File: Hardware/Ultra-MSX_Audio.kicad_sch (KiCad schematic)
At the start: 25 parts, among them J14 Ultra-AUDIO-daughter, U23 S29GL128S90TFI010, U24 FXMA108, U25 FXMA108, U26 FXMA108, U27 FXMA108, U4 YM2610, U9 DAC_YM3016

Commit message: Finished the VDP-board, finished up the mixer-section, removed the buffer-pins from the FPGA, and instead added external buffers for the slots, designed a marquee-block with the Ultra-MSX logo, designed the logotype, andmultiple other changes.
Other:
- note added: "SPI to Parallel (for using modern ROM's) https://highfieldtales.wordpress.com/2011/12/04/very-fast-spi-to-parallel-interface-for-netduino/ -- FPGA-implementation of YM2610: https://github.com/jotego/jt12 YM3016: The YM3015 is nearly identical, except voltage-levels, hence it can be used to figure out a replacement. http://gendev.spritesmind.net/forum/viewtopic.php?t=386&start=180"
- note removed: "SPI to Parallel (for using modern ROM's) https://highfieldtales.wordpress.com/2011/12/04/very-fast-spi-to-parallel-interface-for-netduino/ How to build an Audio mixer: https://www.circuitlib.com/index.php/tutorials/product/39-how-to-build-an-audio-mixer How to inject Mono into Stereo-output; Build a Virtual Earth Summing Amp "Make sure you use linear taper pots for the pans and audio taper pots f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"

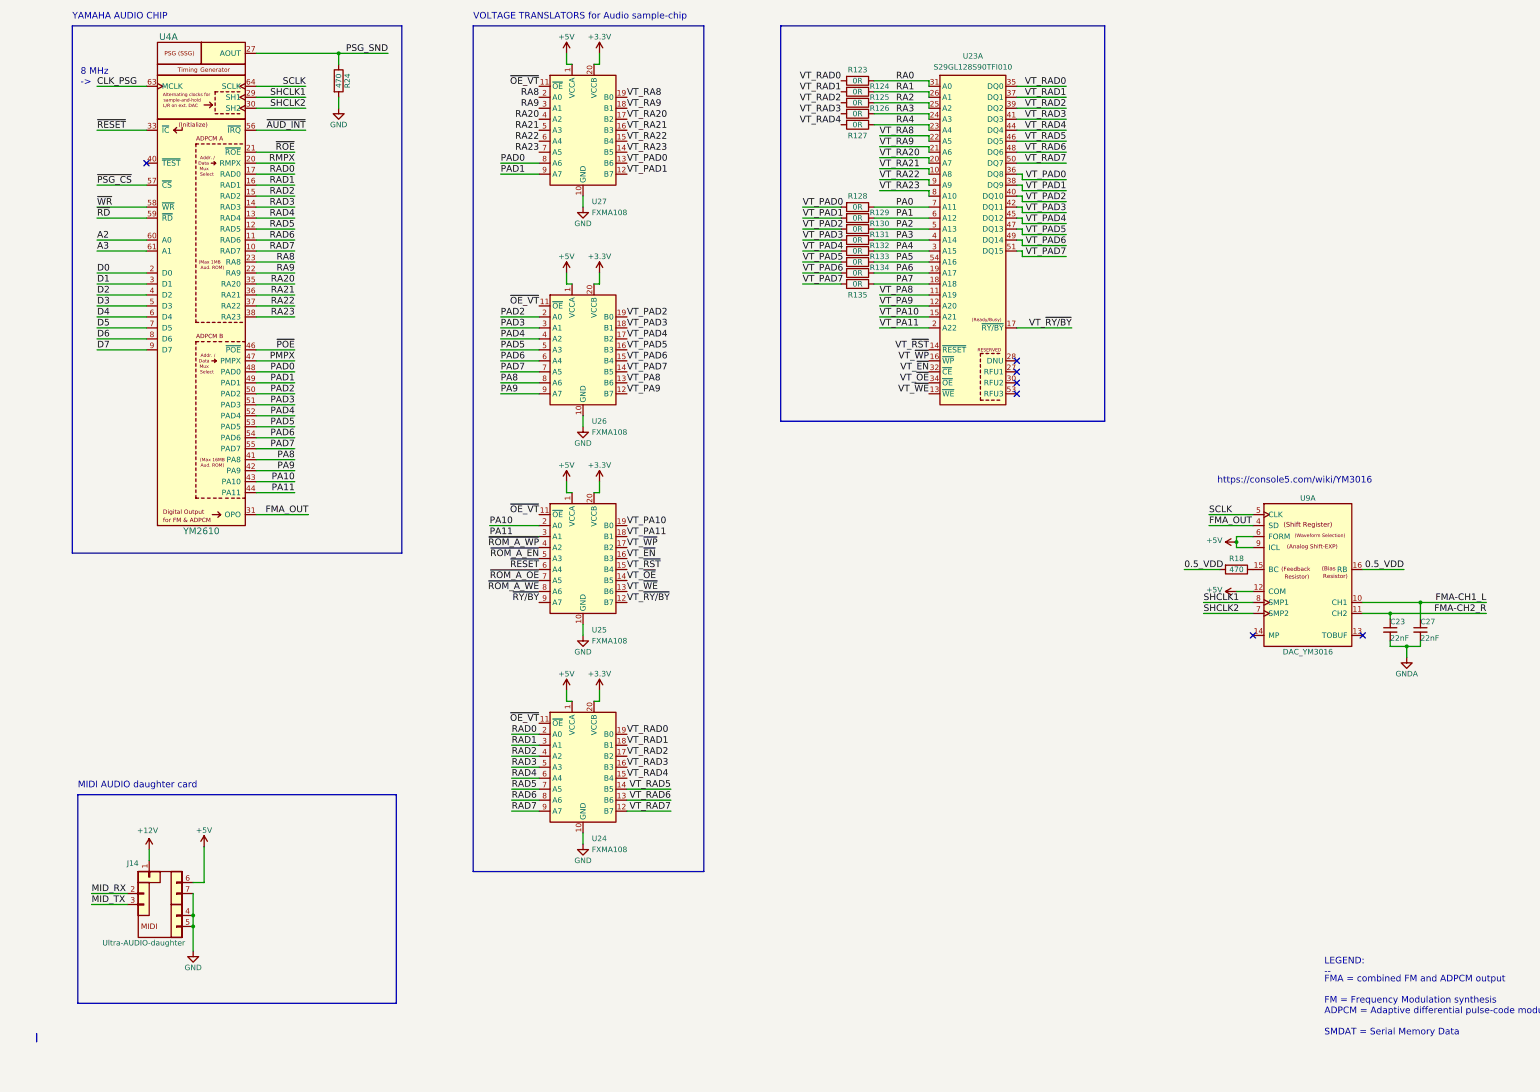
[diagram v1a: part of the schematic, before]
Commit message: Added SD-card slot, made basic 3d-model for sd-card slot, connected it up in the schematic, and numerous other tweaks.
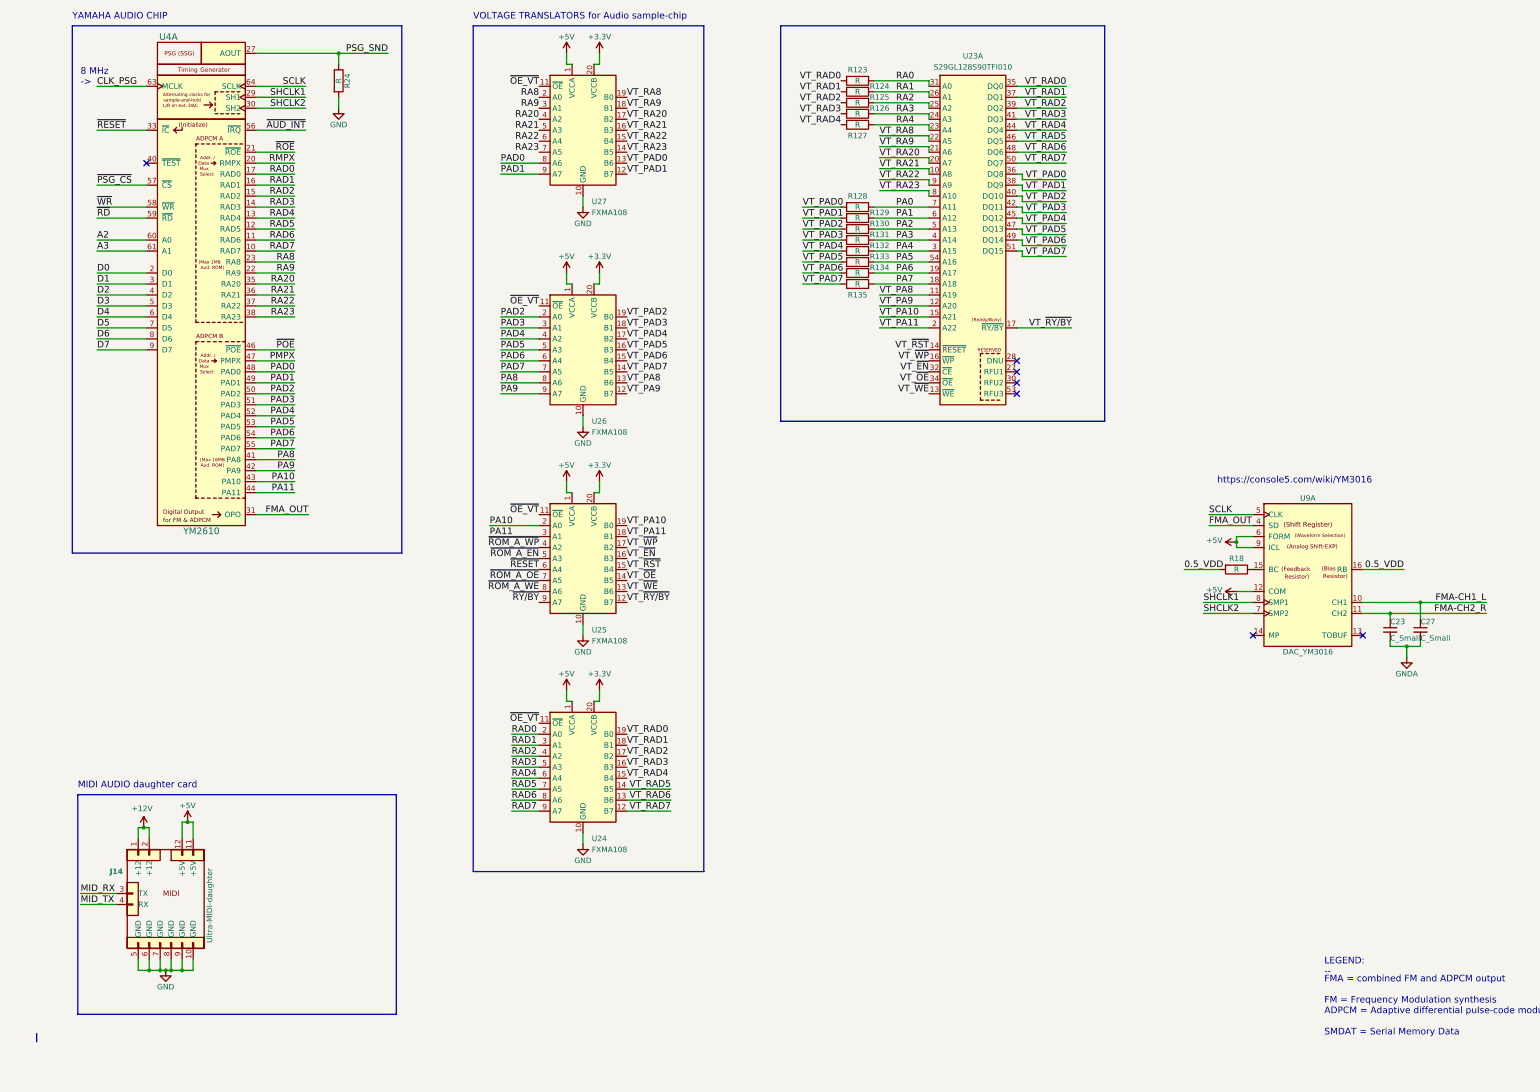
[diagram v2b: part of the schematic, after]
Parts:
- C23, C27: value 22nF -> C_Small
- J14: value Ultra-AUDIO-daughter -> Ultra-MIDI-daughter; footprint Ultra-MSX:Ultra-AUDIO-daughter -> Ultra-MSX:Ultra-MIDI-daughter; symbol Ultra-MSX:Ultra-AUDIO-daughter -> Ultra-MSX:Ultra-MIDI-daughter
- R123, R124, R125, R126, R127, R128, R129, R130, R131, R132, R133, R134, R135: value 0R -> R
- R18, R24: value 470 -> R
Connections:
- net +12V: now also J14.2 (+12)
- net +5V: now also J14.11 (+5V), J14.12 (+5V); no longer J14.6 (Pin_6)
- net GND: now also J14.10 (GND), J14.6 (GND), J14.8 (GND), J14.9 (GND); no longer J14.4 (Pin_4)
- net MID_RX: now also J14.3 (TX); no longer J14.2 (Pin_2)
- net MID_TX: now also J14.4 (RX); no longer J14.3 (Pin_3)

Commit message: Redesigned VDP-board to include a socket, increased it to 4 layers. Various clean-ups here and there. Improved the printer-port and joystick-port 3D-models. Improved the cooling-fin 3D-model, and added attachment-spring in 3D-model.
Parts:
- added J16: Waveblaster_header_02x13, Connector_PinHeader_2.54mm:PinHeader_2x13_P2.54mm_Vertical_SMD, symbol Ultra-MSX:Waveblaster_header_02x13
- added J17: X2GS, Ultra-MSX:X2GS, symbol Ultra-MSX:X2GS
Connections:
- net +12V: now also J16.17 (+12V), J16.21 (+12V)
- net +5V: now also J16.13 (+5V), J16.5 (+5V), J16.9 (+5V)
- net GND: now also J16.10 (GND), J16.12 (GND), J16.2 (GND), J16.4 (GND), J16.6 (GND), J16.8 (GND)
- net GNDA: now also J16.16 (GNDA), J16.18 (GNDA), J16.20 (GNDA), J16.22 (GNDA), J16.24 (GNDA), J16.26 (GNDA)
- net ~{RESET}: no longer U4.33 (~{IC})
- new net WAVE_L: J16.23 (AUD_L)
- new net WAVE_R: J16.19 (AUD_R)
- new net ~{AUD_RST}: J16.25 (~{RST}), U4.33 (~{IC})
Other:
- note added: "1. YAMAHA AUDIO CHIP"
- note added: "2. VOLTAGE TRANSLATORS for Audio sample-chip"
- note added: "3. Audio SAMPLE-chip"
- note added: "4. YAMAHA DAC"
- note added: "LEGEND: ------"
- note added: "SPI to Parallel (for using modern ROM's) https://highfieldtales.wordpress.com/2011/12/04/very-fast-spi-to-parallel-interface-for-netduino/ -- FPGA-implementation of YM2610: https://github.com/jotego/jt12 -- MSX-Midi: http://map.grauw.nl/resources/midi/msx-midi.php -- YM3016: The YM3015 is nearly identical, except voltage-levels, hence it can be used to figure out a replacement. http://gendev.spri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"
- note removed: "LEGEND: --"
- note removed: "SPI to Parallel (for using modern ROM's) https://highfieldtales.wordpress.com/2011/12/04/very-fast-spi-to-parallel-interface-for-netduino/ -- FPGA-implementation of YM2610: https://github.com/jotego/jt12 YM3016: The YM3015 is nearly identical, except voltage-levels, hence it can be used to figure out a replacement. http://gendev.spritesmind.net/forum/viewtopic.php?t=386&start=180"
- note removed: "VOLTAGE TRANSLATORS for Audio sample-chip"
- note removed: "YAMAHA AUDIO CHIP"
- moved on the sheet: C23, C27, J14, R18, U4A, U9A

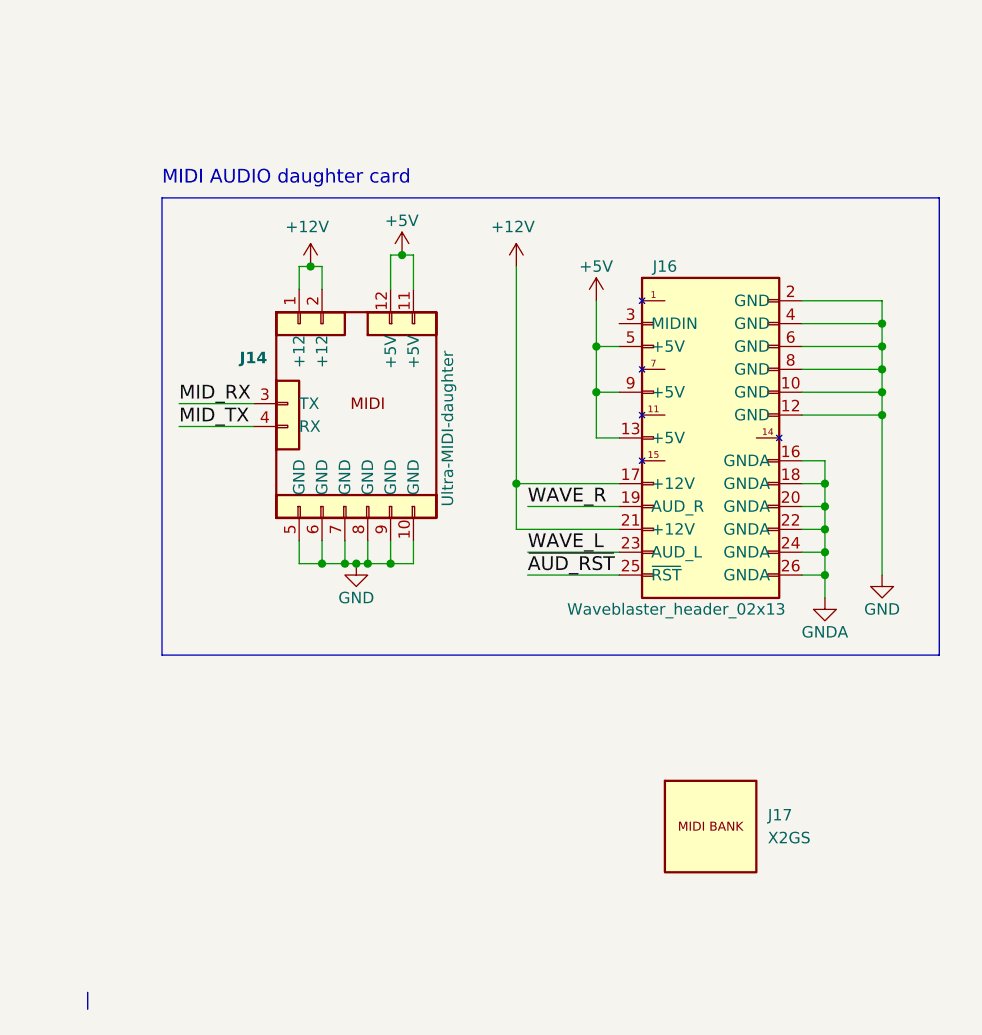
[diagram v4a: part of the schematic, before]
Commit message: Redesigning of the IO-shield, to make room for Keyboard, power and USB.
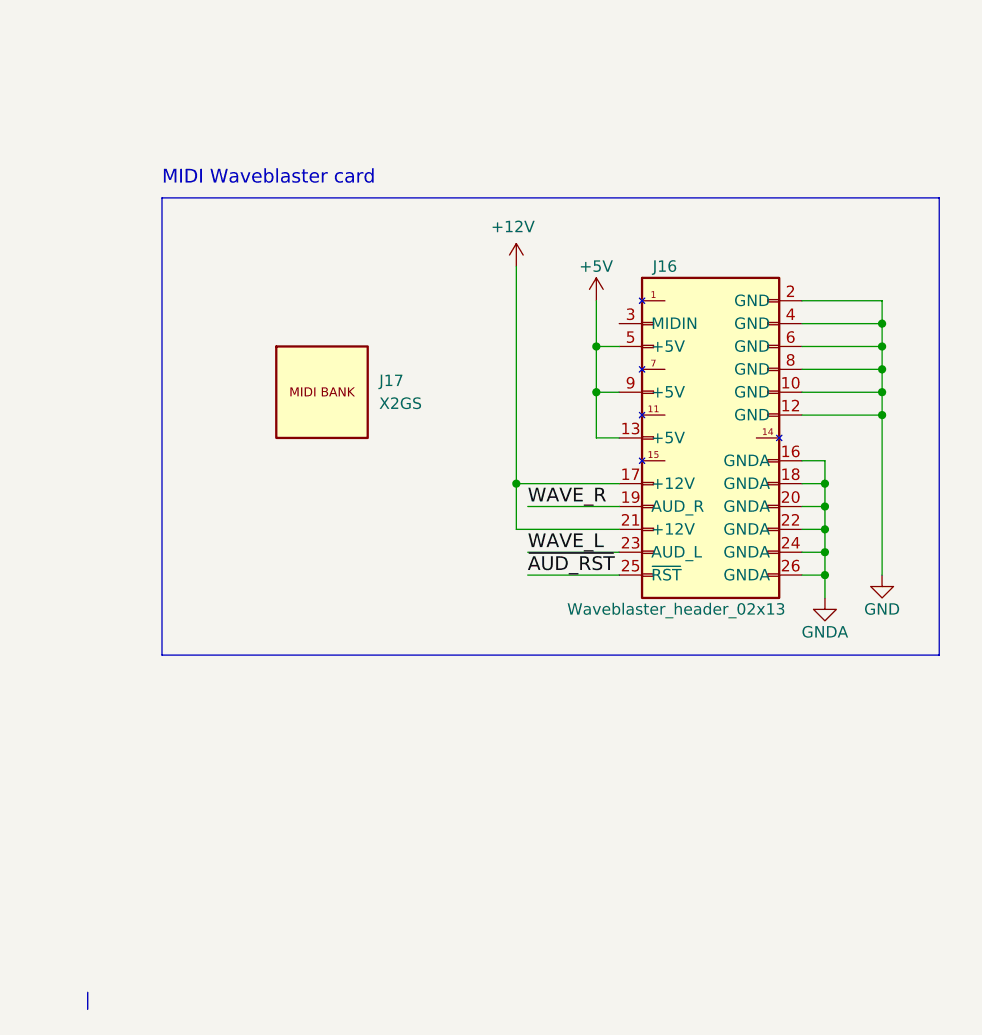
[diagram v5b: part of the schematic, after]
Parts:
- removed J14: Ultra-MIDI-daughter, Ultra-MSX:Ultra-MIDI-daughter, symbol Ultra-MSX:Ultra-MIDI-daughter
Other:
- note added: "MIDI Waveblaster card"
- note removed: "MIDI AUDIO daughter card"
- moved on the sheet: J17

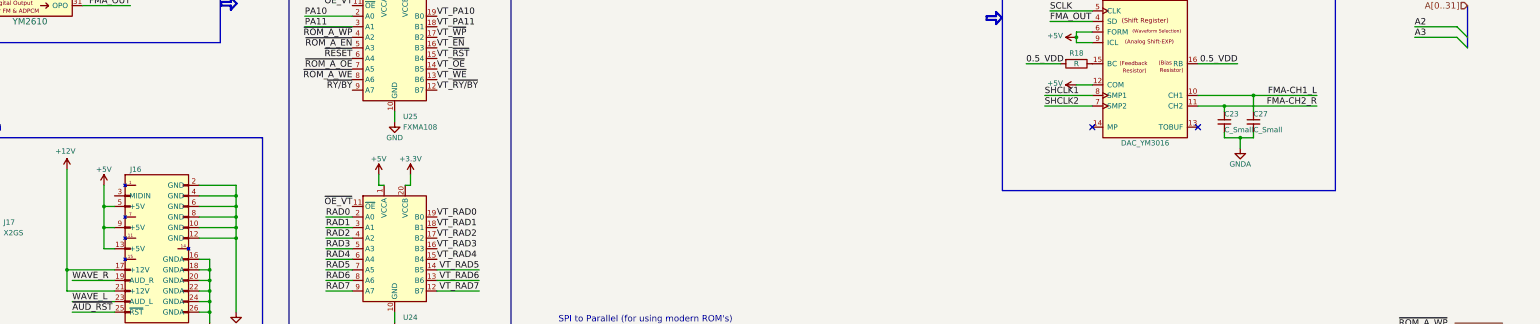
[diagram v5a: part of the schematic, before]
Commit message: Multiple redesigns of the IO-shield. Replaced FPGA with lower pin-count AT10K, since the higher pin-count one is now obsolete.
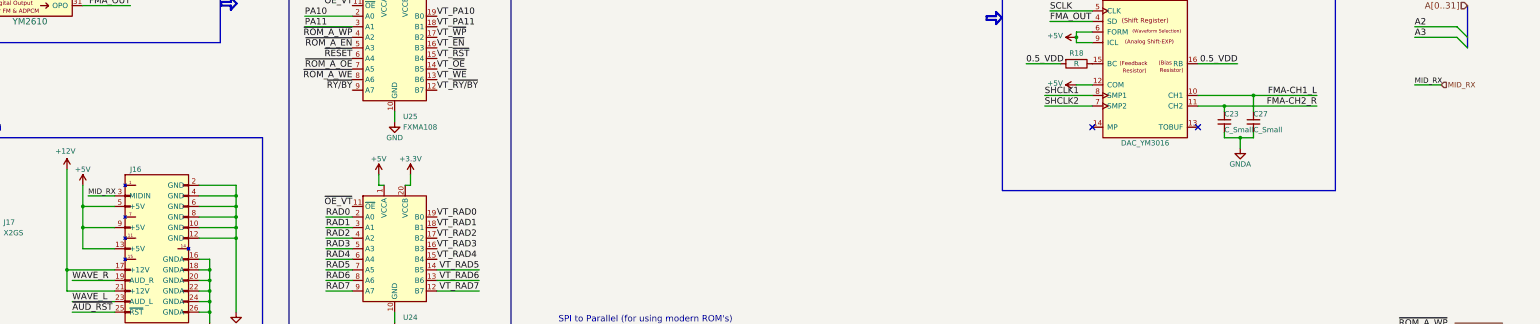
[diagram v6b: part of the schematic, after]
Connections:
- net MID_RX: now reaches J16.3 (MIDIN)
- net +3V3 renamed +3.3V
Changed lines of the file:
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@@
   (junction (at 100.33 179.07) (diameter 0) (color 0 0 0 0)
   )
-  (junction (at 68.58 181.61) (diameter 0) (color 0 0 0 0)
+  (junction (at 63.5 181.61) (diameter 0) (color 0 0 0 0)
   )
   (junction (at 81.915 26.67) (diameter 0) (color 0 0 0 0)
   )
-  (junction (at 68.58 186.69) (diameter 0) (color 0 0 0 0)
-  )
   (junction (at 100.33 181.61) (diameter 0) (color 0 0 0 0)
   )
@@
   )
   (junction (at 93.98 204.47) (diameter 0) (color 0 0 0 0)
+  )
+  (junction (at 63.5 186.69) (diameter 0) (color 0 0 0 0)
   )
   (no_connect (at 238.76 97.79))
@@
     (stroke (width 0) (type default) (color 0 0 0 0))
   )
-  (wire (pts (xy 68.58 181.61) (xy 68.58 186.69))
+  (wire (pts (xy 63.5 181.61) (xy 63.5 186.69))
     (stroke (width 0) (type default) (color 0 0 0 0))
   )
@@
     (stroke (width 0.5) (type solid) (color 0 0 0 0))
   )
-  (wire (pts (xy 68.58 186.69) (xy 71.12 186.69))
+  (wire (pts (xy 63.5 186.69) (xy 71.12 186.69))
     (stroke (width 0) (type default) (color 0 0 0 0))
   )
@@
     (stroke (width 0.5) (type solid) (color 0 0 0 0))
   )
-  (wire (pts (xy 68.58 186.69) (xy 68.58 191.77))
+  (wire (pts (xy 63.5 186.69) (xy 63.5 191.77))
     (stroke (width 0) (type default) (color 0 0 0 0))
   )
@@
     (stroke (width 0) (type default) (color 0 0 0 0))
   )
-  (wire (pts (xy 68.58 191.77) (xy 71.12 191.77))
+  (wire (pts (xy 63.5 191.77) (xy 71.12 191.77))
     (stroke (width 0) (type default) (color 0 0 0 0))
   )
@@
     (stroke (width 0) (type default) (color 0 0 0 0))
   )
-  (wire (pts (xy 68.58 176.53) (xy 68.58 181.61))
+  (wire (pts (xy 63.5 176.53) (xy 63.5 181.61))
     (stroke (width 0) (type default) (color 0 0 0 0))
   )
@@
     (stroke (width 0) (type default) (color 0 0 0 0))
   )
+  (wire (pts (xy 383.54 152.4) (xy 389.89 152.4))
+    (stroke (width 0) (type default) (color 0 0 0 0))
+  )
   (wire (pts (xy 205.74 80.01) (xy 218.44 80.01))
     (stroke (width 0) (type default) (color 0 0 0 0))
@@
     (stroke (width 0) (type default) (color 0 0 0 0))
   )
-  (wire (pts (xy 68.58 181.61) (xy 71.12 181.61))
+  (wire (pts (xy 63.5 181.61) (xy 71.12 181.61))
     (stroke (width 0) (type default) (color 0 0 0 0))
   )
@@
   )
   (wire (pts (xy 387.35 44.45) (xy 378.46 44.45))
+    (stroke (width 0) (type default) (color 0 0 0 0))
+  )
+  (wire (pts (xy 64.77 179.07) (xy 71.12 179.07))
     (stroke (width 0) (type default) (color 0 0 0 0))
   )
@@
     (effects (font (size 1.524 1.524)) (justify left bottom))
   )
+  (label "MID_RX" (at 383.54 152.4 0)
+    (effects (font (size 1.27 1.27)) (justify left bottom))
+  )
   (label "VT_PAD2" (at 148.59 87.63 0)
     (effects (font (size 1.524 1.524)) (justify left bottom))
@@
   (label "SHCLK2" (at 73.66 39.37 180)
     (effects (font (size 1.524 1.524)) (justify right bottom))
+  )
+  (label "MID_RX" (at 64.77 179.07 0)
+    (effects (font (size 1.27 1.27)) (justify left bottom))
   )
   (label "VT_RAD1" (at 250.19 36.83 180)
@@
   (hierarchical_label "~{AUD_INT}" (shape output) (at 389.89 49.53 0)
     (effects (font (size 1.524 1.524)) (justify left))
+  )
+  (hierarchical_label "MID_RX" (shape input) (at 389.89 152.4 0)
+    (effects (font (size 1.27 1.27)) (justify left))
   )
   (hierarchical_label "~{WR}" (shape input) (at 388.62 27.94 0)
@@
     (pin "1")
   )
-  (symbol (lib_id "power:+5V") (at 68.58 176.53 0) (unit 1)
+  (symbol (lib_id "power:+5V") (at 63.5 176.53 0) (unit 1)
     (in_bom yes) (on_board yes)
-    (property "Reference" "#PWR0100" (id 0) (at 68.58 180.34 0)
-      (effects (font (size 1.27 1.27)) hide)
-    )
-    (property "Value" "+5V" (id 1) (at 66.675 172.72 0)
+    (property "Reference" "#PWR0100" (id 0) (at 63.5 180.34 0)
+      (effects (font (size 1.27 1.27)) hide)
+    )
+    (property "Value" "+5V" (id 1) (at 61.595 172.72 0)
       (effects (font (size 1.27 1.27)) (justify left))
     )
-    (property "Footprint" "" (id 2) (at 68.58 176.53 0)
-      (effects (font (size 1.27 1.27)) hide)
-    )
-    (property "Datasheet" "" (id 3) (at 68.58 176.53 0)
-      (effects (font (size 1.27 1.27)) hide)
-    )
+    (property "Footprint" "" (id 2) (at 63.5 176.53 0)
+      (effects (font (size 1.27 1.27)) hide)
+    )
+    (property "Datasheet" "" (id 3) (at 63.5 176.53 0)
+      (effects (font (size 1.27 1.27)) hide)
+    )
